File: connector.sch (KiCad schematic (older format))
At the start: 1 part

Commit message: .
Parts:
- gave numbers to parts that had none: 1
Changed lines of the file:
@@
 $EndDescr
 $Comp
-L CONN_01X06 P?
+L CONN_01X06 P3
 U 1 1 57AF467D
 P 3400 4150
-F 0 "P?" H 3478 4191 50  0000 L CNN
+F 0 "P3" H 3478 4191 50  0000 L CNN
 F 1 "CONN_01X06" H 3478 4100 50  0000 L CNN
-F 2 "" H 3400 4150 50  0000 C CNN
+F 2 "" H 3400 4150 50  0001 C CNN
 F 3 "" H 3400 4150 50  0000 C CNN
 	1    3400 4150
@@
 $EndComp
 $Comp
-L VIN #PWR?
+L VIN #PWR052
 U 1 1 57AF4ABC
 P 3050 3800
-F 0 "#PWR?" H 3050 3650 50  0001 C CNN
+F 0 "#PWR052" H 3050 3650 50  0001 C CNN
 F 1 "VIN" H 3065 3973 50  0000 C CNN
 F 2 "" H 3050 3800 60  0000 C CNN
@@
 	3050 3900 3050 3800
 $Comp
-L GND #PWR?
+L GND #PWR053
 U 1 1 57AF4B0E
 P 3050 4600
-F 0 "#PWR?" H 3050 4350 50  0001 C CNN
+F 0 "#PWR053" H 3050 4350 50  0001 C CNN
 F 1 "GND" H 3055 4427 50  0000 C CNN
 F 2 "" H 3050 4600 50  0000 C CNN

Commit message: Reset circuit, minor changes
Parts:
- renumbered P3 to P?
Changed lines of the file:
@@
 $EndDescr
 $Comp
-L CONN_01X06 P3
+L CONN_01X06 P?
 U 1 1 57AF467D
 P 3400 4150
-F 0 "P3" H 3478 4191 50  0000 L CNN
+F 0 "P?" H 3478 4191 50  0000 L CNN
 F 1 "CONN_01X06" H 3478 4100 50  0000 L CNN
 F 2 "" H 3400 4150 50  0001 C CNN
@@
 $EndComp
 $Comp
-L VIN #PWR052
+L VIN #PWR?
 U 1 1 57AF4ABC
 P 3050 3800
-F 0 "#PWR052" H 3050 3650 50  0001 C CNN
+F 0 "#PWR?" H 3050 3650 50  0001 C CNN
 F 1 "VIN" H 3065 3973 50  0000 C CNN
 F 2 "" H 3050 3800 60  0000 C CNN
@@
 	3050 3900 3050 3800
 $Comp
-L GND #PWR053
+L GND #PWR?
 U 1 1 57AF4B0E
 P 3050 4600
-F 0 "#PWR053" H 3050 4350 50  0001 C CNN
+F 0 "#PWR?" H 3050 4350 50  0001 C CNN
 F 1 "GND" H 3055 4427 50  0000 C CNN
 F 2 "" H 3050 4600 50  0000 C CNN

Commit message: Bom
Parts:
- gave numbers to parts that had none: 1
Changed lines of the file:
@@
 $EndDescr
 $Comp
-L CONN_01X06 P?
+L CONN_01X06 P3
 U 1 1 57AF467D
 P 3400 4150
-F 0 "P?" H 3478 4191 50  0000 L CNN
+F 0 "P3" H 3478 4191 50  0000 L CNN
 F 1 "CONN_01X06" H 3478 4100 50  0000 L CNN
 F 2 "" H 3400 4150 50  0001 C CNN
@@
 $EndComp
 $Comp
-L VIN #PWR?
+L VIN #PWR054
 U 1 1 57AF4ABC
 P 3050 3800
-F 0 "#PWR?" H 3050 3650 50  0001 C CNN
+F 0 "#PWR054" H 3050 3650 50  0001 C CNN
 F 1 "VIN" H 3065 3973 50  0000 C CNN
 F 2 "" H 3050 3800 60  0000 C CNN
@@
 	3050 3900 3050 3800
 $Comp
-L GND #PWR?
+L GND #PWR055
 U 1 1 57AF4B0E
 P 3050 4600
-F 0 "#PWR?" H 3050 4350 50  0001 C CNN
+F 0 "#PWR055" H 3050 4350 50  0001 C CNN
 F 1 "GND" H 3055 4427 50  0000 C CNN
 F 2 "" H 3050 4600 50  0000 C CNN

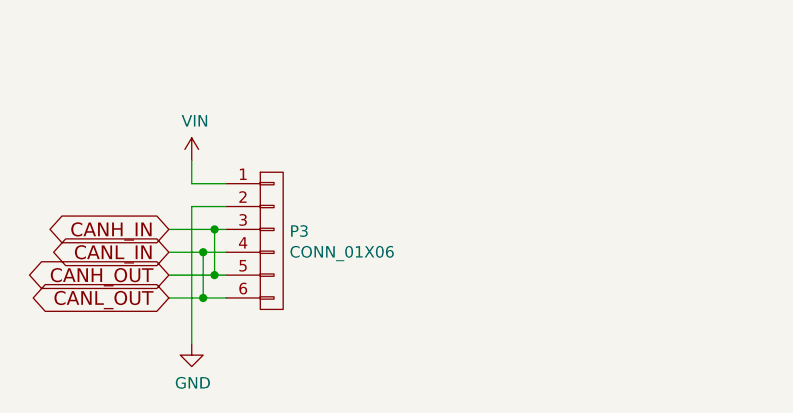
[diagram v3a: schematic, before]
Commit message: Finish BOM, assign and add packages, set connectors, minor changes
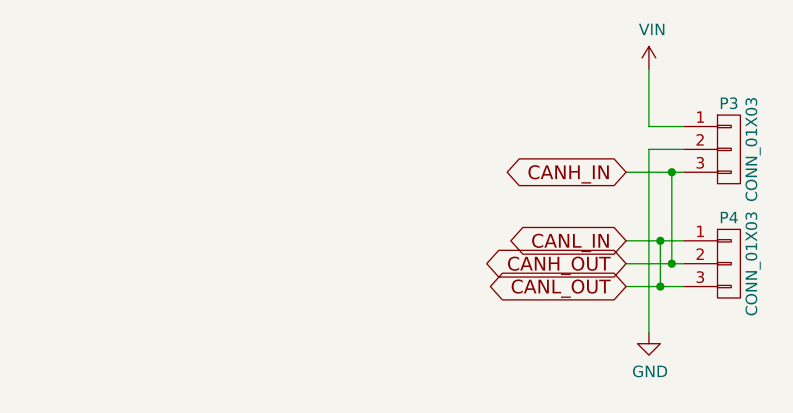
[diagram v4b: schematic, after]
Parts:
- removed P3: CONN_01X06, symbol CONN_01X06
- added P3, P4: CONN_01X03, CAN_Node:WAGO_2060-1423, symbol CONN_01X03
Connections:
- net CANH_IN: now also P3.3 (P3), P4.2 (P2)
- net CANL_IN: now also P4.1 (P1), P4.3 (P3)
- net GND: now also P3.2 (P2)
- net VIN: now also P3.1 (P1)
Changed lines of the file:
@@
 $EndDescr
 $Comp
-L CONN_01X06 P3
-U 1 1 57AF467D
-P 3400 4150
-F 0 "P3" H 3478 4191 50  0000 L CNN
-F 1 "CONN_01X06" H 3478 4100 50  0000 L CNN
-F 2 "" H 3400 4150 50  0001 C CNN
-F 3 "" H 3400 4150 50  0000 C CNN
-	1    3400 4150
+L CONN_01X03 P3
+U 1 1 5811BA7A
+P 5400 3750
+F 0 "P3" H 5400 3950 50  0000 C CNN
+F 1 "CONN_01X03" V 5500 3750 50  0000 C CNN
+F 2 "CAN_Node:WAGO_2060-1423" H 5400 3750 50  0001 C CNN
+F 3 "" H 5400 3750 50  0000 C CNN
+	1    5400 3750
 	1    0    0    -1
 $EndComp
 $Comp
-L VIN #PWR054
-U 1 1 57AF4ABC
-P 3050 3800
-F 0 "#PWR054" H 3050 3650 50  0001 C CNN
-F 1 "VIN" H 3065 3973 50  0000 C CNN
-F 2 "" H 3050 3800 60  0000 C CNN
-F 3 "" H 3050 3800 60  0000 C CNN
-	1    3050 3800
+L CONN_01X03 P4
+U 1 1 5811BADB
+P 5400 4250
+F 0 "P4" H 5400 4450 50  0000 C CNN
+F 1 "CONN_01X03" V 5500 4250 50  0000 C CNN
+F 2 "CAN_Node:WAGO_2060-1423" H 5400 4250 50  0001 C CNN
+F 3 "" H 5400 4250 50  0000 C CNN
+	1    5400 4250
+	1    0    0    -1
+$EndComp
+$Comp
+L GND #PWR054
+U 1 1 5811BC18
+P 5050 4550
+F 0 "#PWR054" H 5050 4300 50  0001 C CNN
+F 1 "GND" H 5055 4377 50  0000 C CNN
+F 2 "" H 5050 4550 50  0000 C CNN
+F 3 "" H 5050 4550 50  0000 C CNN
+	1    5050 4550
+	1    0    0    -1
+$EndComp
+Text GLabel 4950 4150 0    60   BiDi ~ 0
+CANL_IN
+Text GLabel 4950 4250 0    60   BiDi ~ 0
+CANH_OUT
+Text GLabel 4950 4350 0    60   BiDi ~ 0
+CANL_OUT
+Text GLabel 4950 3850 0    60   BiDi ~ 0
+CANH_IN
+$Comp
+L VIN #PWR055
+U 1 1 5811BC4F
+P 5050 3400
+F 0 "#PWR055" H 5050 3250 50  0001 C CNN
+F 1 "VIN" H 5065 3573 50  0000 C CNN
+F 2 "" H 5050 3400 60  0000 C CNN
+F 3 "" H 5050 3400 60  0000 C CNN
+	1    5050 3400
 	1    0    0    -1
 $EndComp
 Wire Wire Line
-	3200 3900 3050 3900
+	4950 4150 5200 4150
 Wire Wire Line
-	3050 3900 3050 3800
-$Comp
-L GND #PWR055
-U 1 1 57AF4B0E
-P 3050 4600
-F 0 "#PWR055" H 3050 4350 50  0001 C CNN
-F 1 "GND" H 3055 4427 50  0000 C CNN
-F 2 "" H 3050 4600 50  0000 C CNN
-F 3 "" H 3050 4600 50  0000 C CNN
-	1    3050 4600
-	1    0    0    -1
-$EndComp
+	4950 4250 5200 4250
 Wire Wire Line
-	3200 4000 3050 4000
+	4950 4350 5200 4350
 Wire Wire Line
-	3050 4000 3050 4600
-Text GLabel 2950 4100 0    60   BiDi ~ 0
-CANH_IN
-Text GLabel 2950 4200 0    60   BiDi ~ 0
-CANL_IN
-Text GLabel 2950 4300 0    60   BiDi ~ 0
-CANH_OUT
-Text GLabel 2950 4400 0    60   BiDi ~ 0
-CANL_OUT
+	5050 4550 5050 3750
 Wire Wire Line
-	2950 4100 3200 4100
+	5050 3750 5200 3750
 Wire Wire Line
-	2950 4200 3200 4200
+	5200 3650 5050 3650
 Wire Wire Line
-	2950 4300 3200 4300
+	5050 3650 5050 3400
 Wire Wire Line
-	2950 4400 3200 4400
+	4950 3850 5200 3850
 Wire Wire Line
-	3150 4100 3150 4300
-Connection ~ 3150 4300
-Connection ~ 3150 4100
+	5100 4150 5100 4350
+Connection ~ 5100 4350
+Connection ~ 5100 4150
 Wire Wire Line
-	3100 4200 3100 4400
-Connection ~ 3100 4400
-Connection ~ 3100 4200
+	5150 4250 5150 3850
+Connection ~ 5150 3850
+Connection ~ 5150 4250
 $EndSCHEMATC

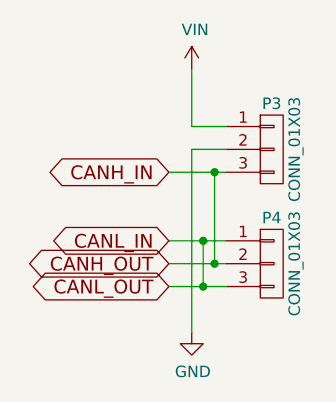
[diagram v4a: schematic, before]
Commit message: Use WAGO 218-106 connector
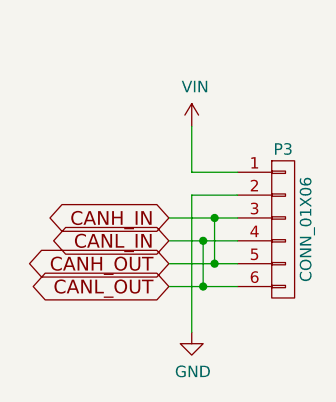
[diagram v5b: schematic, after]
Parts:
- removed P3, P4: CONN_01X03, CAN_Node:WAGO_2060-1423, symbol CONN_01X03
- added P3: CONN_01X06, CAN_Node:WAGO_218-106, symbol CONN_01X06
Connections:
- net CANH_IN: now also P3.3 (P3), P3.5 (P5)
- net CANL_IN: now also P3.4 (P4), P3.6 (P6)
- net GND: now also P3.2 (P2)
- net VIN: now also P3.1 (P1)
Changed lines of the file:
@@
 $EndDescr
-$Comp
-L CONN_01X03 P3
-U 1 1 5811BA7A
-P 5400 3750
-F 0 "P3" H 5400 3950 50  0000 C CNN
-F 1 "CONN_01X03" V 5500 3750 50  0000 C CNN
-F 2 "CAN_Node:WAGO_2060-1423" H 5400 3750 50  0001 C CNN
-F 3 "" H 5400 3750 50  0000 C CNN
-	1    5400 3750
-	1    0    0    -1
-$EndComp
-$Comp
-L CONN_01X03 P4
-U 1 1 5811BADB
-P 5400 4250
-F 0 "P4" H 5400 4450 50  0000 C CNN
-F 1 "CONN_01X03" V 5500 4250 50  0000 C CNN
-F 2 "CAN_Node:WAGO_2060-1423" H 5400 4250 50  0001 C CNN
-F 3 "" H 5400 4250 50  0000 C CNN
-	1    5400 4250
-	1    0    0    -1
-$EndComp
 $Comp
 L GND #PWR054
@@
 Text GLabel 4950 4350 0    60   BiDi ~ 0
 CANL_OUT
-Text GLabel 4950 3850 0    60   BiDi ~ 0
+Text GLabel 4950 4050 0    60   BiDi ~ 0
 CANH_IN
 $Comp
 L VIN #PWR055
 U 1 1 5811BC4F
-P 5050 3400
-F 0 "#PWR055" H 5050 3250 50  0001 C CNN
-F 1 "VIN" H 5065 3573 50  0000 C CNN
-F 2 "" H 5050 3400 60  0000 C CNN
-F 3 "" H 5050 3400 60  0000 C CNN
-	1    5050 3400
+P 5050 3650
+F 0 "#PWR055" H 5050 3500 50  0001 C CNN
+F 1 "VIN" H 5065 3823 50  0000 C CNN
+F 2 "" H 5050 3650 60  0000 C CNN
+F 3 "" H 5050 3650 60  0000 C CNN
+	1    5050 3650
 	1    0    0    -1
 $EndComp
 Wire Wire Line
-	4950 4150 5200 4150
+	4950 4150 5250 4150
 Wire Wire Line
-	4950 4250 5200 4250
+	4950 4250 5250 4250
 Wire Wire Line
-	4950 4350 5200 4350
+	4950 4350 5250 4350
 Wire Wire Line
-	5050 4550 5050 3750
+	5050 4550 5050 3950
 Wire Wire Line
-	5050 3750 5200 3750
+	5050 3950 5250 3950
 Wire Wire Line
-	5200 3650 5050 3650
+	5250 3850 5050 3850
 Wire Wire Line
-	5050 3650 5050 3400
+	5050 3850 5050 3650
 Wire Wire Line
-	4950 3850 5200 3850
+	4950 4050 5250 4050
 Wire Wire Line
 	5100 4150 5100 4350
@@
 Connection ~ 5100 4150
 Wire Wire Line
-	5150 4250 5150 3850
-Connection ~ 5150 3850
+	5150 4250 5150 4050
+Connection ~ 5150 4050
 Connection ~ 5150 4250
+$Comp
+L CONN_01X06 P3
+U 1 1 58146F94
+P 5450 4100
+F 0 "P3" H 5450 4450 50  0000 C CNN
+F 1 "CONN_01X06" V 5550 4100 50  0000 C CNN
+F 2 "CAN_Node:WAGO_218-106" H 5450 4100 50  0001 C CNN
+F 3 "" H 5450 4100 50  0000 C CNN
+	1    5450 4100
+	1    0    0    -1
+$EndComp
 $EndSCHEMATC

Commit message: Layout: first version
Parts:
- removed P3: CONN_01X06, CAN_Node:WAGO_218-106, symbol CONN_01X06
- added P3: CONN_01X04, CAN_Node:WAGO_218-104, symbol CONN_01X04
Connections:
- net CANH_IN: now also P3.4 (P4)
- net CANL_IN: now also P3.3 (P3)
- net GND: now also P3.2 (P2)
- net VIN: now also P3.1 (P1)
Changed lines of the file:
@@
 $EndDescr
 $Comp
-L GND #PWR054
+L GND #PWR056
 U 1 1 5811BC18
 P 5050 4550
-F 0 "#PWR054" H 5050 4300 50  0001 C CNN
+F 0 "#PWR056" H 5050 4300 50  0001 C CNN
 F 1 "GND" H 5055 4377 50  0000 C CNN
 F 2 "" H 5050 4550 50  0000 C CNN
@@
 	1    0    0    -1
 $EndComp
+Text GLabel 4950 4050 0    60   BiDi ~ 0
+CANL_IN
 Text GLabel 4950 4150 0    60   BiDi ~ 0
-CANL_IN
-Text GLabel 4950 4250 0    60   BiDi ~ 0
-CANH_OUT
-Text GLabel 4950 4350 0    60   BiDi ~ 0
-CANL_OUT
-Text GLabel 4950 4050 0    60   BiDi ~ 0
 CANH_IN
 $Comp
-L VIN #PWR055
+L VIN #PWR057
 U 1 1 5811BC4F
 P 5050 3650
-F 0 "#PWR055" H 5050 3500 50  0001 C CNN
+F 0 "#PWR057" H 5050 3500 50  0001 C CNN
 F 1 "VIN" H 5065 3823 50  0000 C CNN
 F 2 "" H 5050 3650 60  0000 C CNN
@@
 Wire Wire Line
 	4950 4150 5250 4150
-Wire Wire Line
-	4950 4250 5250 4250
-Wire Wire Line
-	4950 4350 5250 4350
 Wire Wire Line
 	5050 4550 5050 3950
@@
 Wire Wire Line
 	4950 4050 5250 4050
-Wire Wire Line
-	5100 4150 5100 4350
-Connection ~ 5100 4350
-Connection ~ 5100 4150
-Wire Wire Line
-	5150 4250 5150 4050
-Connection ~ 5150 4050
-Connection ~ 5150 4250
 $Comp
-L CONN_01X06 P3
-U 1 1 58146F94
-P 5450 4100
-F 0 "P3" H 5450 4450 50  0000 C CNN
-F 1 "CONN_01X06" V 5550 4100 50  0000 C CNN
-F 2 "CAN_Node:WAGO_218-106" H 5450 4100 50  0001 C CNN
-F 3 "" H 5450 4100 50  0000 C CNN
-	1    5450 4100
+L CONN_01X04 P3
+U 1 1 581AFCAF
+P 5450 4000
+F 0 "P3" H 5450 4250 50  0000 C CNN
+F 1 "CONN_01X04" V 5550 4000 50  0000 C CNN
+F 2 "CAN_Node:WAGO_218-104" H 5450 4000 50  0001 C CNN
+F 3 "" H 5450 4000 50  0000 C CNN
+	1    5450 4000
 	1    0    0    -1
 $EndComp
